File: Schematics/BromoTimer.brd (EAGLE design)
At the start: 49.2 x 71.1 mm, 28 parts, among them IC1 PIC16F687, IC2 7805TV, K1 G2R2A, K2 G2R2A, Q1 BC548B, Q2 BC548B, Q3 BC548B, X1 AC_IN, X4 22-23-2031, X5 AC_OUT

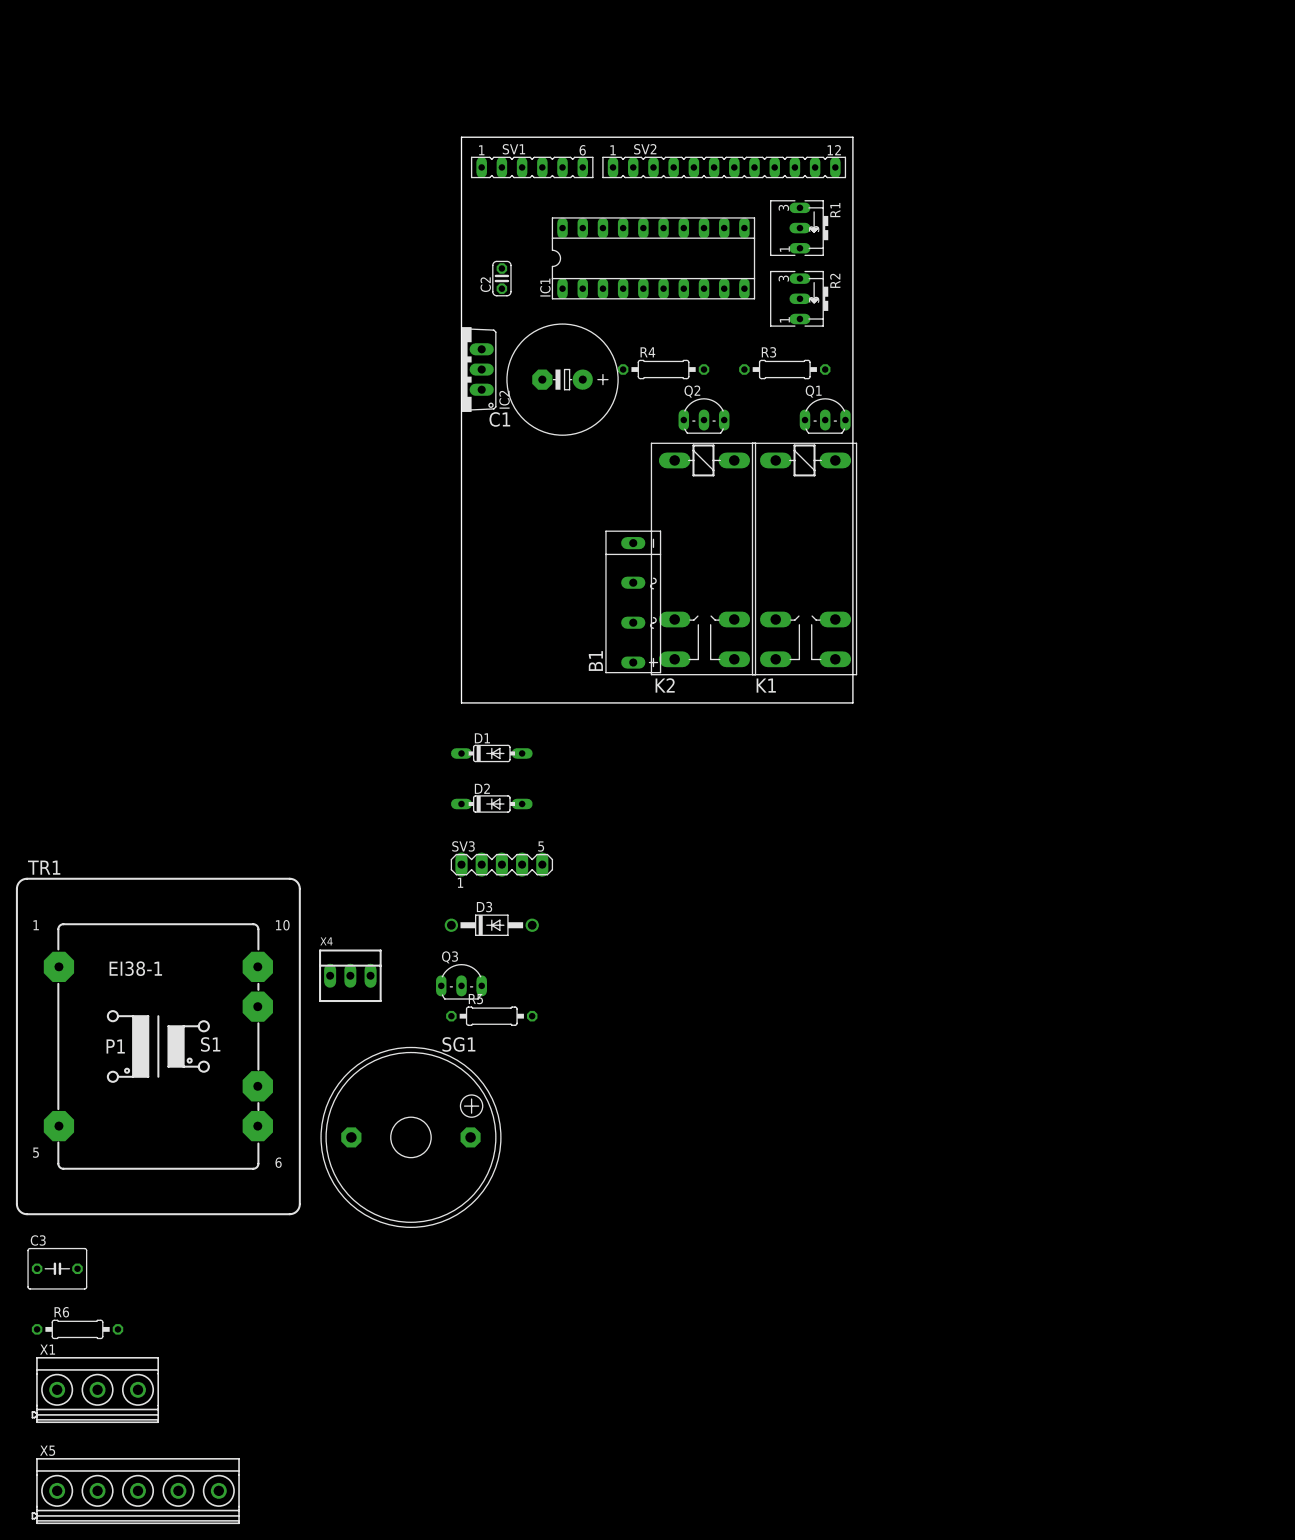
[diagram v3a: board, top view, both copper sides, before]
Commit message: Initial component layout.
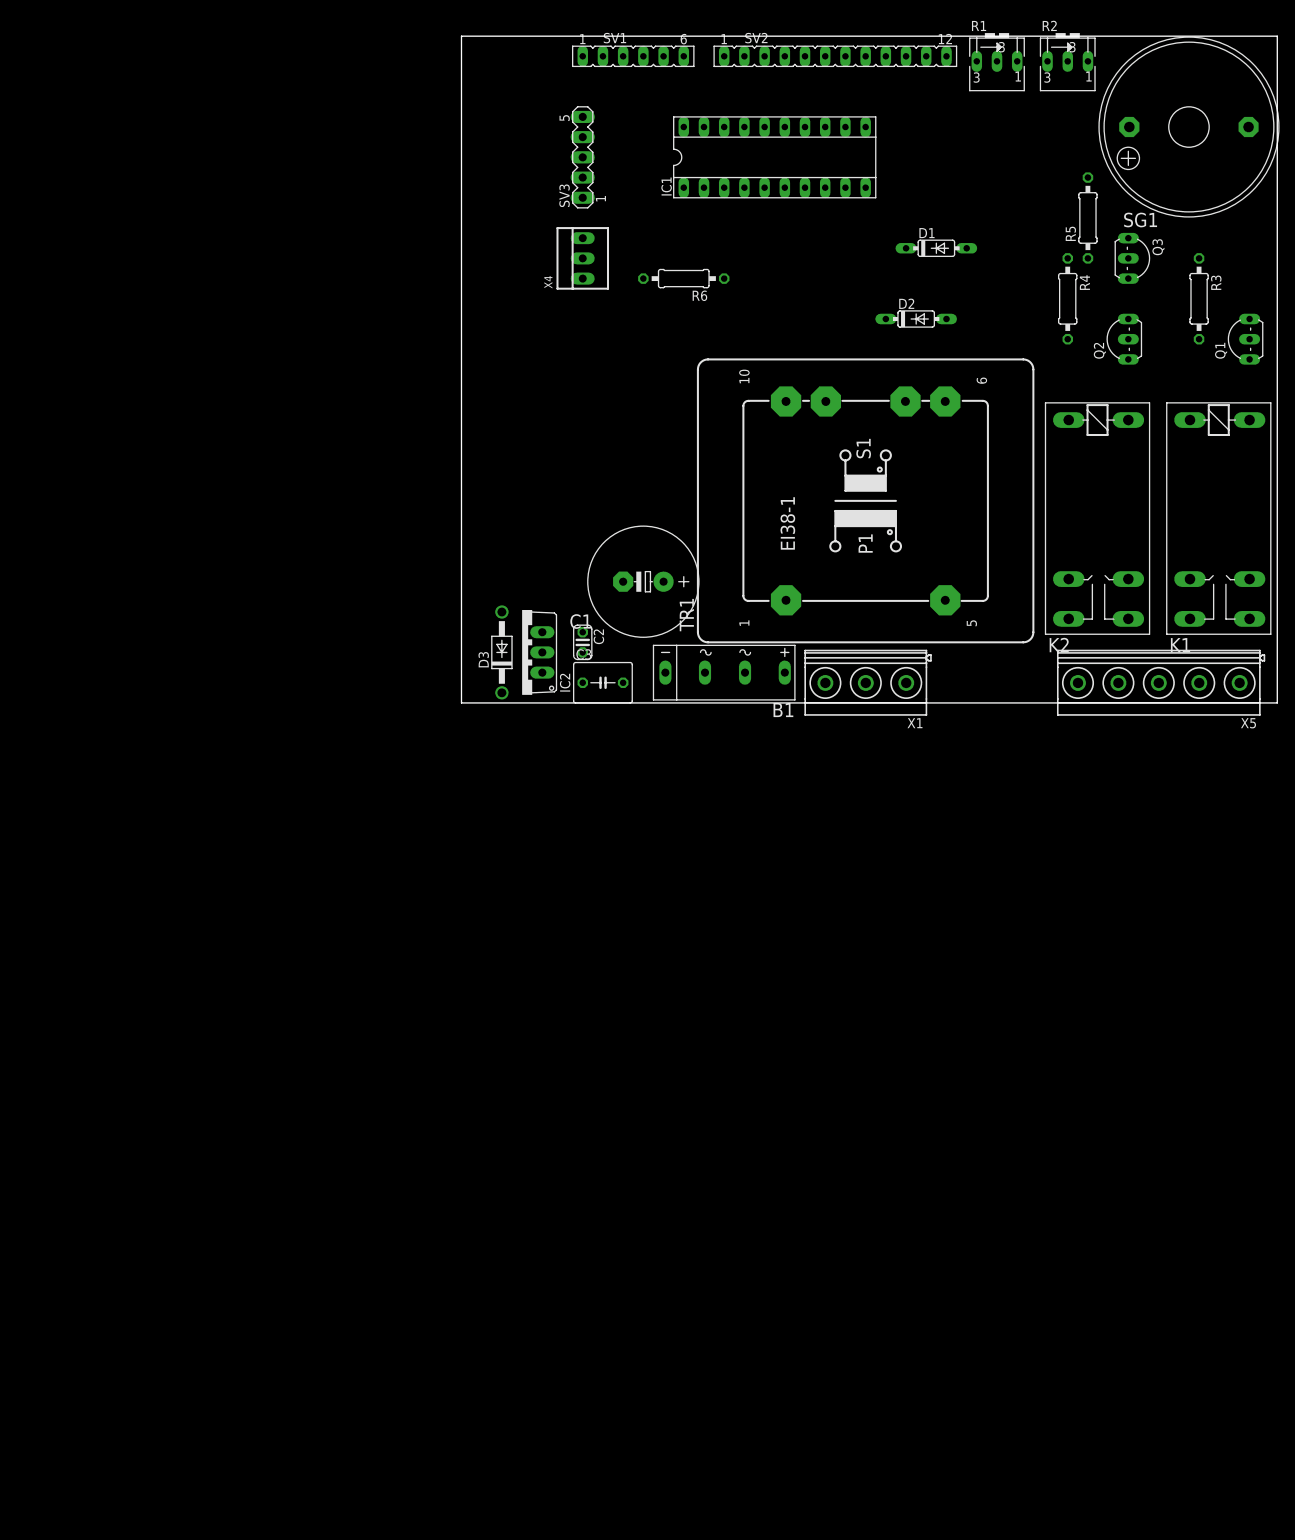
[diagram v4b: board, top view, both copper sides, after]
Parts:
- moved X5 163.6 mm to (87.6, 2.54), turned to 180 degrees
- moved SG1 160.3 mm to (91.4, 72.4), turned to 180 degrees
- moved R6 152.5 mm to (27.9, 53.3), turned to 180 degrees
- moved X1 127.5 mm to (48.3, 2.54), turned to 180 degrees
- moved R5 125.2 mm to (78.7, 61.0), turned to 90 degrees
- moved Q3 124.0 mm to (85.1, 55.9), turned to 270 degrees
- moved TR1 112.3 mm to (50.8, 25.4), turned to 90 degrees
- moved C3 100.6 mm to (17.8, 2.54)
- moved X4 94.8 mm to (15.2, 55.9), turned to 90 degrees
- moved SV3 89.5 mm to (15.2, 68.6), turned to 90 degrees
- moved D1 84.6 mm to (59.7, 57.1)
- moved D2 81.0 mm to (57.1, 48.3)
- moved Q1 52.8 mm to (97.8, 45.7), turned to 90 degrees
- moved Q2 52.8 mm to (82.5, 45.7), turned to 90 degrees
- moved R3 52.8 mm to (92.7, 50.8), turned to 270 degrees
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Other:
- board size 49.2 x 71.1 mm -> 102.5 x 83.8 mm

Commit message: Fix some ERC errors
Come traces were not connected on the transformer, R1 and R2 were missing
values, so was TR1.
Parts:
- C3: value (none) -> 330n
- R1, R2: value (none) -> 100k
- R6: value (none) -> 470
- TR1: value (none) -> 220/12
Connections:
- new net N$22: TR1.5, X1.1
- net AC1: no longer X1.1
- net N$12: now also TR1.9
- net N$2: now also TR1.7
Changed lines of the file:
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@@
 <element name="C1" library="rcl" package="E5-13" value="1m" x="22.86" y="15.24" rot="R180"/>
 <element name="C2" library="rcl" package="C025-024X044" value="100n" x="15.24" y="7.62" rot="R270"/>
-<element name="R1" library="pot" package="B25V" value="" x="67.31" y="80.01"/>
-<element name="R2" library="pot" package="B25V" value="" x="76.2" y="80.01"/>
+<element name="R1" library="pot" package="B25V" value="100k" x="67.31" y="80.01"/>
+<element name="R2" library="pot" package="B25V" value="100k" x="76.2" y="80.01"/>
 <element name="Q1" library="transistor-npn" package="TO92-EBC" value="BC548B" x="97.79" y="45.72" rot="R90"/>
 <element name="Q2" library="transistor-npn" package="TO92-EBC" value="BC548B" x="82.55" y="45.72" rot="R90"/>
@@
 <attribute name="OC_FARNELL" value="unknown" x="91.44" y="72.39" size="1.778" layer="27" rot="R180" display="off"/>
 </element>
-<element name="TR1" library="trafo" package="EI38-1" value="" x="50.8" y="25.4" rot="R90"/>
-<element name="C3" library="rcl" package="C050-050X075" value="" x="17.78" y="2.54"/>
-<element name="R6" library="rcl" package="0207/10" value="" x="27.94" y="53.34" rot="R180"/>
+<element name="TR1" library="trafo" package="EI38-1" value="220/12" x="50.8" y="25.4" rot="R90"/>
+<element name="C3" library="rcl" package="C050-050X075" value="330n" x="17.78" y="2.54"/>
+<element name="R6" library="rcl" package="0207/10" value="470" x="27.94" y="53.34" rot="R180"/>
 <element name="X1" library="con-phoenix-508" package="MKDSN1,5/3-5,08" value="AC_IN" x="48.26" y="2.54" rot="R180">
 <attribute name="OC_NEWARK" value="70R0299" x="48.26" y="2.54" size="1.778" layer="27" rot="R180" display="off"/>
@@
 <contactref element="K1" pad="P2"/>
 <contactref element="K2" pad="P2"/>
-<contactref element="X1" pad="1"/>
 <wire x1="76.327" y1="15.5702" x2="91.567" y2="15.5702" width="0" layer="19" extent="1-1"/>
-<wire x1="55.9011" y1="2.515" x2="76.327" y2="15.5702" width="0" layer="19" extent="1-1"/>
-</signal>
-<signal name="N$2">
-<contactref element="B1" pad="AC2"/>
 </signal>
 <signal name="N$12">
 <contactref element="B1" pad="AC1"/>
+<contactref element="TR1" pad="9"/>
+<wire x1="35.6362" y1="3.81" x2="45.7962" y2="37.8968" width="0" layer="19" extent="1-1"/>
 </signal>
 <signal name="V+">
@@
 <wire x1="15.24" y1="53.34" x2="22.86" y2="53.34" width="0" layer="19" extent="1-1"/>
 </signal>
+<signal name="N$2">
+<contactref element="B1" pad="AC2"/>
+<contactref element="TR1" pad="7"/>
+<wire x1="30.607" y1="3.81" x2="55.8038" y2="37.8968" width="0" layer="19" extent="1-1"/>
+</signal>
+<signal name="N$22">
+<contactref element="X1" pad="1"/>
+<contactref element="TR1" pad="5"/>
+<wire x1="55.9011" y1="2.515" x2="60.8076" y2="12.9032" width="0" layer="19" extent="1-1"/>
+</signal>
 </signals>

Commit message: Component placement finished
This is just a candidate though. The area with Q1 Q2 and Q3 could get optimized
a little more though...
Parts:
- moved R3 52.2 mm to (40.6, 47.0), turned to 0 degrees
- moved Q1 41.9 mm to (55.9, 47.0)
- moved R5 38.6 mm to (40.6, 54.6), turned to 180 degrees
- moved Q3 35.6 mm to (49.5, 54.6), turned to 90 degrees
- moved R4 35.6 mm to (40.6, 50.8), turned to 0 degrees
- moved Q2 33.0 mm to (49.5, 47.0)
- moved SG1 25.7 mm to (77.5, 50.8), turned to 270 degrees
- moved IC1 25.1 mm to (21.6, 50.8)
- moved X4 24.0 mm to (2.54, 35.6)
- moved R6 23.4 mm to (10.2, 38.1), turned to 270 degrees
- moved SV1 21.8 mm to (8.89, 63.5)
- moved SV3 21.8 mm to (2.54, 50.8)
- moved R2 21.1 mm to (64.8, 62.2)
- moved SV2 21.1 mm to (35.6, 63.5)
- moved R1 20.5 mm to (57.1, 62.2)
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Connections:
- removed net N$22: TR1.5, X1.1
- net AC1: now also TR1.5, X1.1
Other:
- board size 102.5 x 83.8 mm -> 89.8 x 66 mm
